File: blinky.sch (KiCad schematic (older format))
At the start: 40 parts, among them J1 MIC_CLK, J10 DEBUG, J11 SWD, J12 BATTERY, J13 UART, J14 5V, J15 3V3, J2 MIC_DOUT, J3 LED_DIN, J4 ACCEL_MISO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

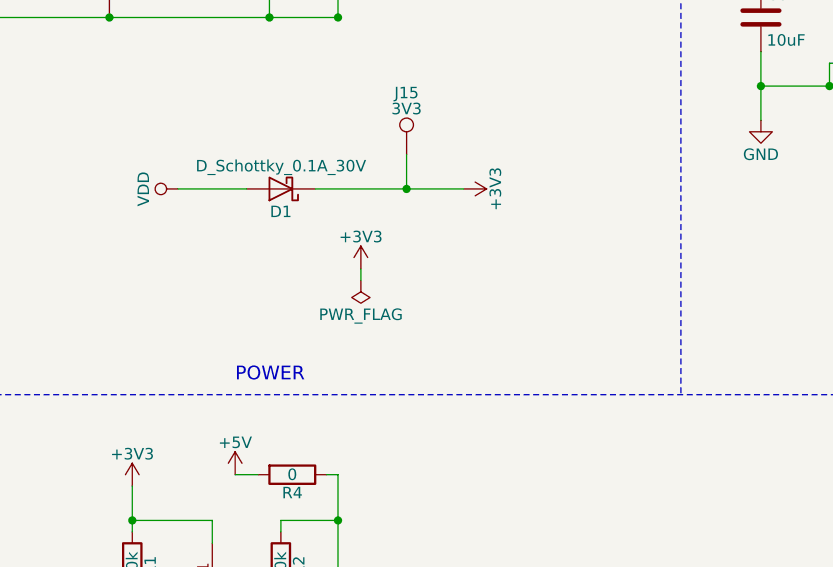
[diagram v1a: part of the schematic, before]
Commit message: Add shortcut to enable 3V3 Only mode
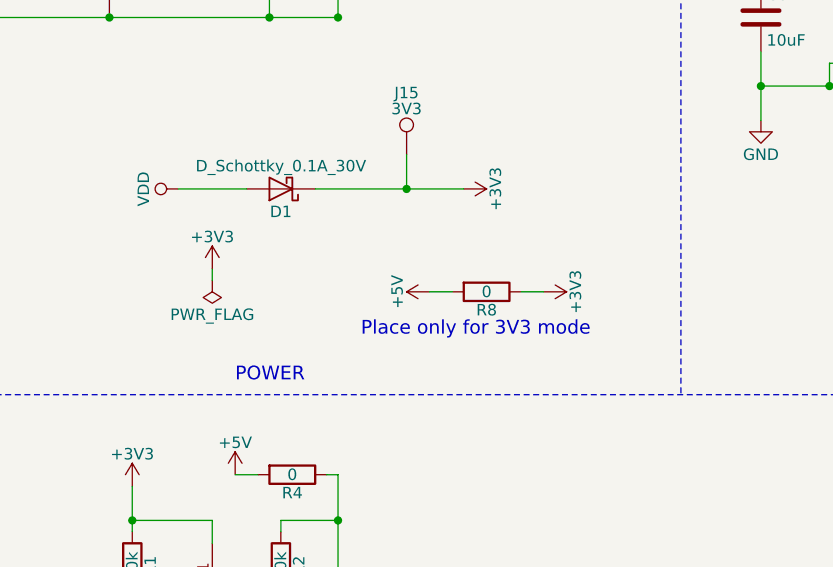
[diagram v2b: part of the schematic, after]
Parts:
- added R8: 0, Resistors_SMD:R_0805, symbol R
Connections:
- net +3V3: now also R8.1
- net +5V: now also R8.2
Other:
- note added: "Place only for 3V3 mode"
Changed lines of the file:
@@
 EESchema Schematic File Version 2
+LIBS:blinky-rescue
 LIBS:power
 LIBS:device
@@
 $EndSheet
 $Comp
-L GND #PWR19
+L GND #PWR01
 U 1 1 59735157
 P 8250 2650
-F 0 "#PWR19" H 8250 2400 50  0001 C CNN
+F 0 "#PWR01" H 8250 2400 50  0001 C CNN
 F 1 "GND" H 8250 2500 50  0000 C CNN
 F 2 "" H 8250 2650 50  0001 C CNN
@@
 $EndComp
 $Comp
-L GND #PWR21
+L GND #PWR02
 U 1 1 59735414
 P 8450 1250
-F 0 "#PWR21" H 8450 1000 50  0001 C CNN
+F 0 "#PWR02" H 8450 1000 50  0001 C CNN
 F 1 "GND" H 8450 1100 50  0000 C CNN
 F 2 "" H 8450 1250 50  0001 C CNN
@@
 $EndComp
 $Comp
-L +5V #PWR8
+L +5V #PWR03
 U 1 1 59735989
 P 5950 4200
-F 0 "#PWR8" H 5950 4050 50  0001 C CNN
+F 0 "#PWR03" H 5950 4050 50  0001 C CNN
 F 1 "+5V" H 5950 4340 50  0000 C CNN
 F 2 "" H 5950 4200 50  0001 C CNN
@@
 $EndComp
 $Comp
-L GND #PWR13
+L GND #PWR04
 U 1 1 597359AA
 P 6400 5400
-F 0 "#PWR13" H 6400 5150 50  0001 C CNN
+F 0 "#PWR04" H 6400 5150 50  0001 C CNN
 F 1 "GND" H 6400 5250 50  0000 C CNN
 F 2 "" H 6400 5400 50  0001 C CNN
@@
 $EndComp
 $Comp
-L GND #PWR9
+L GND #PWR05
 U 1 1 59736818
 P 6000 6250
-F 0 "#PWR9" H 6000 6000 50  0001 C CNN
+F 0 "#PWR05" H 6000 6000 50  0001 C CNN
 F 1 "GND" H 6000 6100 50  0000 C CNN
 F 2 "" H 6000 6250 50  0001 C CNN
@@
 $EndComp
 $Comp
-L VDD #PWR3
+L VDD #PWR06
 U 1 1 5974FA3E
 P 4150 1000
-F 0 "#PWR3" H 4150 850 50  0001 C CNN
+F 0 "#PWR06" H 4150 850 50  0001 C CNN
 F 1 "VDD" H 4150 1150 50  0000 C CNN
 F 2 "" H 4150 1000 50  0001 C CNN
@@
 $EndComp
 $Comp
-L GND #PWR4
+L GND #PWR07
 U 1 1 5974FA44
 P 4150 2300
-F 0 "#PWR4" H 4150 2050 50  0001 C CNN
+F 0 "#PWR07" H 4150 2050 50  0001 C CNN
 F 1 "GND" H 4150 2150 50  0000 C CNN
 F 2 "" H 4150 2300 50  0001 C CNN
@@
 $EndComp
 $Comp
-L +5V #PWR15
+L +5V #PWR08
 U 1 1 5974FA78
 P 6750 1000
-F 0 "#PWR15" H 6750 850 50  0001 C CNN
+F 0 "#PWR08" H 6750 850 50  0001 C CNN
 F 1 "+5V" H 6750 1140 50  0000 C CNN
 F 2 "" H 6750 1000 50  0001 C CNN
@@
 $EndComp
 $Comp
-L +3V3 #PWR16
+L +3V3 #PWR09
 U 1 1 5974FA92
 P 6950 2950
-F 0 "#PWR16" H 6950 2800 50  0001 C CNN
+F 0 "#PWR09" H 6950 2800 50  0001 C CNN
 F 1 "+3V3" H 6950 3090 50  0000 C CNN
 F 2 "" H 6950 2950 50  0001 C CNN
@@
 $EndComp
 $Comp
-L +3V3 #PWR18
+L +3V3 #PWR010
 U 1 1 5974FC09
 P 8250 1900
-F 0 "#PWR18" H 8250 1750 50  0001 C CNN
+F 0 "#PWR010" H 8250 1750 50  0001 C CNN
 F 1 "+3V3" H 8250 2040 50  0000 C CNN
 F 2 "" H 8250 1900 50  0001 C CNN
@@
 $EndComp
 $Comp
-L +3V3 #PWR20
+L +3V3 #PWR011
 U 1 1 5974FD08
 P 8450 800
-F 0 "#PWR20" H 8450 650 50  0001 C CNN
+F 0 "#PWR011" H 8450 650 50  0001 C CNN
 F 1 "+3V3" H 8450 940 50  0000 C CNN
 F 2 "" H 8450 800 50  0001 C CNN
@@
 $EndComp
 $Comp
-L +3V3 #PWR6
+L +3V3 #PWR012
 U 1 1 5974FDE2
 P 5500 4250
-F 0 "#PWR6" H 5500 4100 50  0001 C CNN
+F 0 "#PWR012" H 5500 4100 50  0001 C CNN
 F 1 "+3V3" H 5500 4390 50  0000 C CNN
 F 2 "" H 5500 4250 50  0001 C CNN
@@
 $EndComp
 $Comp
-L +3V3 #PWR10
+L +3V3 #PWR013
 U 1 1 5974FF6A
 P 6000 6650
-F 0 "#PWR10" H 6000 6500 50  0001 C CNN
+F 0 "#PWR013" H 6000 6500 50  0001 C CNN
 F 1 "+3V3" H 6000 6790 50  0000 C CNN
 F 2 "" H 6000 6650 50  0001 C CNN
@@
 $EndComp
 $Comp
-L +3V3 #PWR1
+L +3V3 #PWR014
 U 1 1 59757575
 P 800 1150
-F 0 "#PWR1" H 800 1000 50  0001 C CNN
+F 0 "#PWR014" H 800 1000 50  0001 C CNN
 F 1 "+3V3" H 800 1290 50  0000 C CNN
 F 2 "" H 800 1150 50  0001 C CNN
@@
 $EndComp
 $Comp
-L GND #PWR2
+L GND #PWR015
 U 1 1 59757983
 P 800 2000
-F 0 "#PWR2" H 800 1750 50  0001 C CNN
+F 0 "#PWR015" H 800 1750 50  0001 C CNN
 F 1 "GND" H 800 1850 50  0000 C CNN
 F 2 "" H 800 2000 50  0001 C CNN
@@
 $EndComp
 $Comp
-L VDD #PWR12
+L VDD #PWR016
 U 1 1 597763DE
 P 6300 7200
-F 0 "#PWR12" H 6300 7050 50  0001 C CNN
+F 0 "#PWR016" H 6300 7050 50  0001 C CNN
 F 1 "VDD" H 6300 7350 50  0000 C CNN
 F 2 "" H 6300 7200 50  0001 C CNN
@@
 $EndComp
 $Comp
-L GND #PWR11
+L GND #PWR017
 U 1 1 59776525
 P 6250 7350
-F 0 "#PWR11" H 6250 7100 50  0001 C CNN
+F 0 "#PWR017" H 6250 7100 50  0001 C CNN
 F 1 "GND" H 6250 7200 50  0000 C CNN
 F 2 "" H 6250 7350 50  0001 C CNN
@@
 $EndComp
 $Comp
-L PWR_FLAG #FLG1
+L PWR_FLAG #FLG018
 U 1 1 59776D41
 P 6250 7250
-F 0 "#FLG1" H 6250 7325 50  0001 C CNN
+F 0 "#FLG018" H 6250 7325 50  0001 C CNN
 F 1 "PWR_FLAG" H 6250 7400 50  0000 C CNN
 F 2 "" H 6250 7250 50  0001 C CNN
@@
 $EndComp
 $Comp
-L +3V3 #PWR14
+L +3V3 #PWR019
 U 1 1 5977B020
-P 6500 3300
-F 0 "#PWR14" H 6500 3150 50  0001 C CNN
-F 1 "+3V3" H 6500 3440 50  0000 C CNN
-F 2 "" H 6500 3300 50  0001 C CNN
-F 3 "" H 6500 3300 50  0001 C CNN
-	1    6500 3300
-	1    0    0    -1
-$EndComp
-$Comp
-L PWR_FLAG #FLG2
+P 5850 3300
+F 0 "#PWR019" H 5850 3150 50  0001 C CNN
+F 1 "+3V3" H 5850 3440 50  0000 C CNN
+F 2 "" H 5850 3300 50  0001 C CNN
+F 3 "" H 5850 3300 50  0001 C CNN
+	1    5850 3300
+	1    0    0    -1
+$EndComp
+$Comp
+L PWR_FLAG #FLG020
 U 1 1 5977B2DF
-P 6500 3350
-F 0 "#FLG2" H 6500 3425 50  0001 C CNN
-F 1 "PWR_FLAG" H 6500 3500 50  0000 C CNN
-F 2 "" H 6500 3350 50  0001 C CNN
-F 3 "" H 6500 3350 50  0001 C CNN
-	1    6500 3350
+P 5850 3350
+F 0 "#FLG020" H 5850 3425 50  0001 C CNN
+F 1 "PWR_FLAG" H 5850 3500 50  0000 C CNN
+F 2 "" H 5850 3350 50  0001 C CNN
+F 3 "" H 5850 3350 50  0001 C CNN
+	1    5850 3350
 	-1   0    0    1
 $EndComp
@@
 	5100 7250 5150 7250
 $Comp
-L GND #PWR5
+L GND #PWR021
 U 1 1 59DAA5B4
 P 5100 7100
-F 0 "#PWR5" H 5100 6850 50  0001 C CNN
+F 0 "#PWR021" H 5100 6850 50  0001 C CNN
 F 1 "GND" H 5100 6950 50  0000 C CNN
 F 2 "" H 5100 7100 50  0001 C CNN
@@
 $EndComp
 Wire Wire Line
-	6500 3350 6500 3300
+	5850 3350 5850 3300
 $Comp
 L R R4
@@
 	6050 4200 5950 4200
 $Comp
-L VDD #PWR7
+L VDD #PWR022
 U 1 1 5A04A8BB
 P 5700 2950
-F 0 "#PWR7" H 5700 2800 50  0001 C CNN
+F 0 "#PWR022" H 5700 2800 50  0001 C CNN
 F 1 "VDD" H 5700 3100 50  0000 C CNN
 F 2 "" H 5700 2950 50  0001 C CNN
@@
 $EndComp
 $Comp
-L GND #PWR17
+L GND #PWR023
 U 1 1 5A1E106E
 P 7750 5900
-F 0 "#PWR17" H 7750 5650 50  0001 C CNN
+F 0 "#PWR023" H 7750 5650 50  0001 C CNN
 F 1 "GND" H 7750 5750 50  0000 C CNN
 F 2 "" H 7750 5900 50  0001 C CNN
@@
 Wire Wire Line
 	8950 5900 8650 5900
+$Comp
+L +5V #PWR024
+U 1 1 5A2DE8A0
+P 6800 3400
+F 0 "#PWR024" H 6800 3250 50  0001 C CNN
+F 1 "+5V" H 6800 3540 50  0000 C CNN
+F 2 "" H 6800 3400 50  0001 C CNN
+F 3 "" H 6800 3400 50  0001 C CNN
+	1    6800 3400
+	0    -1   -1   0
+$EndComp
+$Comp
+L +3V3 #PWR025
+U 1 1 5A2DE9EF
+P 7300 3400
+F 0 "#PWR025" H 7300 3250 50  0001 C CNN
+F 1 "+3V3" H 7300 3540 50  0000 C CNN
+F 2 "" H 7300 3400 50  0001 C CNN
+F 3 "" H 7300 3400 50  0001 C CNN
+	1    7300 3400
+	0    1    1    0
+$EndComp
+$Comp
+L R R8
+U 1 1 5A2DEB42
+P 7050 3400
+F 0 "R8" V 7130 3400 50  0000 C CNN
+F 1 "0" V 7050 3400 50  0000 C CNN
+F 2 "Resistors_SMD:R_0805" V 6980 3400 50  0001 C CNN
+F 3 "" H 7050 3400 50  0001 C CNN
+F 4 "YAGEO" H 1550 -1200 50  0001 C CNN "MFR"
+F 5 "RC0805JR-070RL" H 1550 -1200 50  0001 C CNN "MPN"
+F 6 "Mouser" H 1550 -1200 50  0001 C CNN "SPR"
+F 7 "603-RC0805JR-070RL" H 1550 -1200 50  0001 C CNN "SPN"
+	1    7050 3400
+	0    1    1    0
+$EndComp
+Wire Wire Line
+	6900 3400 6800 3400
+Wire Wire Line
+	7200 3400 7300 3400
+Text Notes 6500 3600 0    60   ~ 0
+Place only for 3V3 mode
 $EndSCHEMATC

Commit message: change level shifter
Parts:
- removed Q1: BSS138, TO_SOT_Packages_SMD:SOT-23, symbol BSS138
- removed R4: 0, Resistors_SMD:R_0603, symbol R
- added C19: 100nF, Capacitors_SMD:C_0603, symbol C
- added C20, C21: NA, Capacitors_SMD:C_0603, symbol C
- added J16, J17: GS2, Connectors:GS2, symbol GS2
- added U5: TXS0101, TO_SOT_Packages_SMD:SOT-23-6, symbol TXS0101
- R1, R2: value 10k -> NA; MFR YAGEOq -> (none); MPN RC0603JR-0710KL -> (none); PN RC0603FR-0710KL -> (none); SPN 603-RC0603JR-0710KL -> (none); SPR Mouser -> (none)
- renumbered R8 to R4
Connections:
- net +3V3: now also C19.2, J16.1 (G1), U5.1 (VCCA); no longer R4.1
- net +5V: now also J16.2 (G2)
- net GND: now also C19.1, C20.1, C21.2, U5.2 (GND)
- net LED_DATAIN: now also J17.2 (G2), U5.3 (A); no longer R1.2
- net LED5V_DATAIN: now reaches P1.1 (DataIn), R2.2
- net LED5V_DATAIN: now also C21.1, J17.1 (G1), U5.4 (B)
- net LED_5V: now reaches P1.2 (5V), P2.2 (5V), P3.2 (5V), P4.2 (5V), P5.2 (5V), R2.1
- net LED_5V: now also R4.1, C20.2, U5.6 (VCCB)
- new net: R1.2, U5.5 (OE)
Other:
- moved on the sheet: D2, P1, P2, P3, P4, P5, R4, R5

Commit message: uses 2mm pitch pin header for neopixel
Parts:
- P1, P2, P3, P4, P5: footprint Pin_Headers:Pin_Header_Straight_1x04 -> Pin_Headers:Pin_Header_Straight_1x04_Pitch2.00mm
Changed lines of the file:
@@
 F 0 "P1" H 6900 4600 50  0000 C CNN
 F 1 "BUTTON" V 7250 4350 50  0000 C CNN
-F 2 "Pin_Headers:Pin_Header_Straight_1x04" H 6900 4350 50  0001 C CNN
+F 2 "Pin_Headers:Pin_Header_Straight_1x04_Pitch2.00mm" H 6900 4350 50  0001 C CNN
 F 3 "" H 6900 4350 50  0000 C CNN
-F 4 "" H 250 -600 50  0001 C CNN "MFR"
-F 5 "" H 250 -600 50  0001 C CNN "MPN"
-F 6 "" H 250 -600 50  0001 C CNN "SPR"
-F 7 "" H 250 -600 50  0001 C CNN "SPN"
-F 8 "" H 250 -600 50  0001 C CNN "SPURL"
 	1    6900 4350
 	1    0    0    -1
@@
 F 0 "P2" H 7850 4600 50  0000 C CNN
 F 1 "BUTTON" V 8200 4350 50  0000 C CNN
-F 2 "Pin_Headers:Pin_Header_Straight_1x04" H 7850 4350 50  0001 C CNN
+F 2 "Pin_Headers:Pin_Header_Straight_1x04_Pitch2.00mm" H 7850 4350 50  0001 C CNN
 F 3 "" H 7850 4350 50  0000 C CNN
-F 4 "" H 250 -600 50  0001 C CNN "MFR"
-F 5 "" H 250 -600 50  0001 C CNN "MPN"
-F 6 "" H 250 -600 50  0001 C CNN "SPR"
-F 7 "" H 250 -600 50  0001 C CNN "SPN"
-F 8 "" H 250 -600 50  0001 C CNN "SPURL"
 	1    7850 4350
 	1    0    0    -1
@@
 F 0 "P3" H 8800 4600 50  0000 C CNN
 F 1 "BUTTON" V 9150 4350 50  0000 C CNN
-F 2 "Pin_Headers:Pin_Header_Straight_1x04" H 8800 4350 50  0001 C CNN
+F 2 "Pin_Headers:Pin_Header_Straight_1x04_Pitch2.00mm" H 8800 4350 50  0001 C CNN
 F 3 "" H 8800 4350 50  0000 C CNN
-F 4 "" H 250 -600 50  0001 C CNN "MFR"
-F 5 "" H 250 -600 50  0001 C CNN "MPN"
-F 6 "" H 250 -600 50  0001 C CNN "SPR"
-F 7 "" H 250 -600 50  0001 C CNN "SPN"
-F 8 "" H 250 -600 50  0001 C CNN "SPURL"
 	1    8800 4350
 	1    0    0    -1
@@
 F 0 "P4" H 9750 4600 50  0000 C CNN
 F 1 "BUTTON" V 10100 4350 50  0000 C CNN
-F 2 "Pin_Headers:Pin_Header_Straight_1x04" H 9750 4350 50  0001 C CNN
+F 2 "Pin_Headers:Pin_Header_Straight_1x04_Pitch2.00mm" H 9750 4350 50  0001 C CNN
 F 3 "" H 9750 4350 50  0000 C CNN
-F 4 "" H 250 -600 50  0001 C CNN "MFR"
-F 5 "" H 250 -600 50  0001 C CNN "MPN"
-F 6 "" H 250 -600 50  0001 C CNN "SPR"
-F 7 "" H 250 -600 50  0001 C CNN "SPN"
-F 8 "" H 250 -600 50  0001 C CNN "SPURL"
 	1    9750 4350
 	1    0    0    -1
@@
 F 0 "P5" H 10700 4600 50  0000 C CNN
 F 1 "BUTTON" V 11050 4350 50  0000 C CNN
-F 2 "Pin_Headers:Pin_Header_Straight_1x04" H 10700 4350 50  0001 C CNN
+F 2 "Pin_Headers:Pin_Header_Straight_1x04_Pitch2.00mm" H 10700 4350 50  0001 C CNN
 F 3 "" H 10700 4350 50  0000 C CNN
-F 4 "" H 250 -600 50  0001 C CNN "MFR"
-F 5 "" H 250 -600 50  0001 C CNN "MPN"
-F 6 "" H 250 -600 50  0001 C CNN "SPR"
-F 7 "" H 250 -600 50  0001 C CNN "SPN"
-F 8 "" H 250 -600 50  0001 C CNN "SPURL"
 	1    10700 4350
 	1    0    0    -1

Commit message: new led pin footprints
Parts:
- J12: footprint Pin_Headers:Pin_Header_Straight_1x02 -> Connectors_JST:JST_EH_S02B-EH_02x2.50mm_Angled
- P1, P2, P3, P4, P5: footprint Pin_Headers:Pin_Header_Straight_1x04_Pitch2.00mm -> jfi:Pin_Header_Straight_1_04_Pitch1.25mm
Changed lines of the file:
@@
 EESchema Schematic File Version 2
+LIBS:blinky-rescue
 LIBS:power
 LIBS:device
@@
 F 0 "P1" H 6900 4600 50  0000 C CNN
 F 1 "BUTTON" V 7250 4350 50  0000 C CNN
-F 2 "Pin_Headers:Pin_Header_Straight_1x04_Pitch2.00mm" H 6900 4350 50  0001 C CNN
+F 2 "jfi:Pin_Header_Straight_1_04_Pitch1.25mm" H 6900 4350 50  0001 C CNN
 F 3 "" H 6900 4350 50  0000 C CNN
 	1    6900 4350
@@
 F 0 "P2" H 7850 4600 50  0000 C CNN
 F 1 "BUTTON" V 8200 4350 50  0000 C CNN
-F 2 "Pin_Headers:Pin_Header_Straight_1x04_Pitch2.00mm" H 7850 4350 50  0001 C CNN
+F 2 "jfi:Pin_Header_Straight_1_04_Pitch1.25mm" H 7850 4350 50  0001 C CNN
 F 3 "" H 7850 4350 50  0000 C CNN
 	1    7850 4350
@@
 F 0 "P3" H 8800 4600 50  0000 C CNN
 F 1 "BUTTON" V 9150 4350 50  0000 C CNN
-F 2 "Pin_Headers:Pin_Header_Straight_1x04_Pitch2.00mm" H 8800 4350 50  0001 C CNN
+F 2 "jfi:Pin_Header_Straight_1_04_Pitch1.25mm" H 8800 4350 50  0001 C CNN
 F 3 "" H 8800 4350 50  0000 C CNN
 	1    8800 4350
@@
 F 0 "P4" H 9750 4600 50  0000 C CNN
 F 1 "BUTTON" V 10100 4350 50  0000 C CNN
-F 2 "Pin_Headers:Pin_Header_Straight_1x04_Pitch2.00mm" H 9750 4350 50  0001 C CNN
+F 2 "jfi:Pin_Header_Straight_1_04_Pitch1.25mm" H 9750 4350 50  0001 C CNN
 F 3 "" H 9750 4350 50  0000 C CNN
 	1    9750 4350
@@
 F 0 "P5" H 10700 4600 50  0000 C CNN
 F 1 "BUTTON" V 11050 4350 50  0000 C CNN
-F 2 "Pin_Headers:Pin_Header_Straight_1x04_Pitch2.00mm" H 10700 4350 50  0001 C CNN
+F 2 "jfi:Pin_Header_Straight_1_04_Pitch1.25mm" H 10700 4350 50  0001 C CNN
 F 3 "" H 10700 4350 50  0000 C CNN
 	1    10700 4350
@@
 F 0 "J12" H 6550 7450 50  0000 C CNN
 F 1 "BATTERY" V 6650 7300 50  0000 C CNN
-F 2 "Pin_Headers:Pin_Header_Straight_1x02" H 6550 7300 50  0001 C CNN
+F 2 "Connectors_JST:JST_EH_S02B-EH_02x2.50mm_Angled" H 6550 7300 50  0001 C CNN
 F 3 "" H 6550 7300 50  0001 C CNN
-F 4 "" H 50  50  50  0001 C CNN "MFR"
-F 5 "" H 50  50  50  0001 C CNN "MPN"
-F 6 "" H 50  50  50  0001 C CNN "SPR"
-F 7 "" H 50  50  50  0001 C CNN "SPN"
-F 8 "" H 50  50  50  0001 C CNN "SPURL"
 	1    6550 7300
 	1    0    0    -1
